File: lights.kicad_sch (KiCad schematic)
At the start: 24 parts, among them Q1 PMV60ENEAR, Q2 PMV60ENEAR

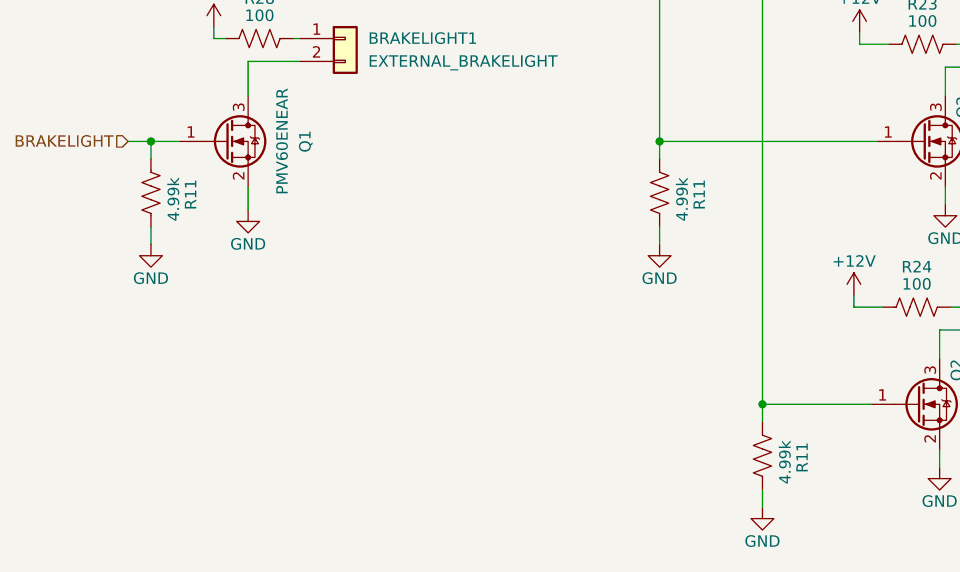
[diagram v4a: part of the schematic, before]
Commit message: organized schematic, changed resistor values, moved ignition signals to IC
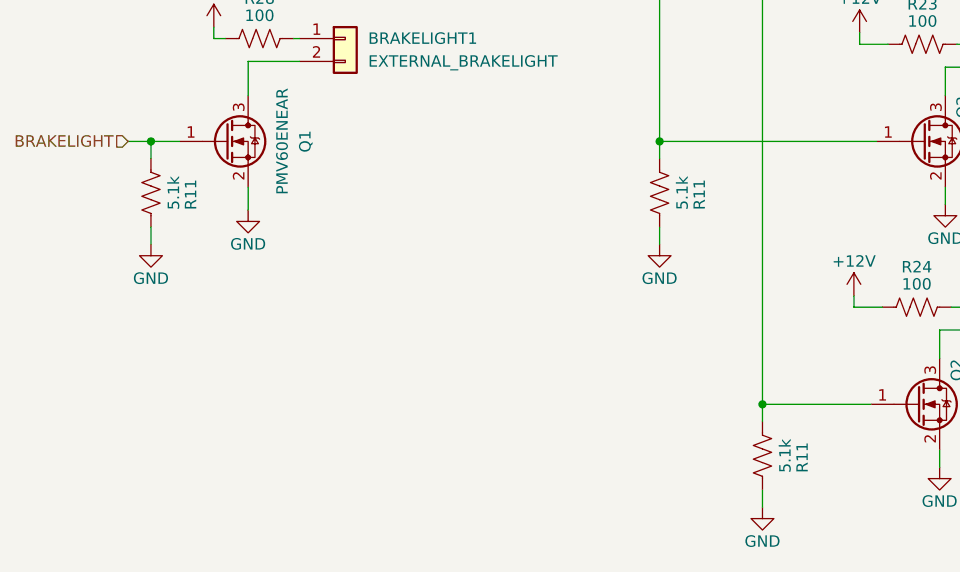
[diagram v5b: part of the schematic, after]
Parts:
- R11: value 4.99k -> 5.1k
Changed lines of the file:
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@@
       (effects (font (size 1.27 1.27)) (justify left))
     )
-    (property "Value" "4.99k" (at 98.425 129.54 90)
+    (property "Value" "5.1k" (at 98.425 128.27 90)
       (effects (font (size 1.27 1.27)) (justify left))
     )
@@
       (effects (font (size 1.27 1.27)) (justify left))
     )
-    (property "Value" "4.99k" (at 154.94 129.54 90)
+    (property "Value" "5.1k" (at 154.94 128.27 90)
       (effects (font (size 1.27 1.27)) (justify left))
     )
@@
       (effects (font (size 1.27 1.27)) (justify left))
     )
-    (property "Value" "4.99k" (at 166.37 158.75 90)
-      (effects (font (size 1.27 1.27)) (justify left))
-    )
+    (property "Value" "5.1k" (at 166.37 157.48 90)
+      (effects (font (size 1.27 1.27)) (justify left))
+    )

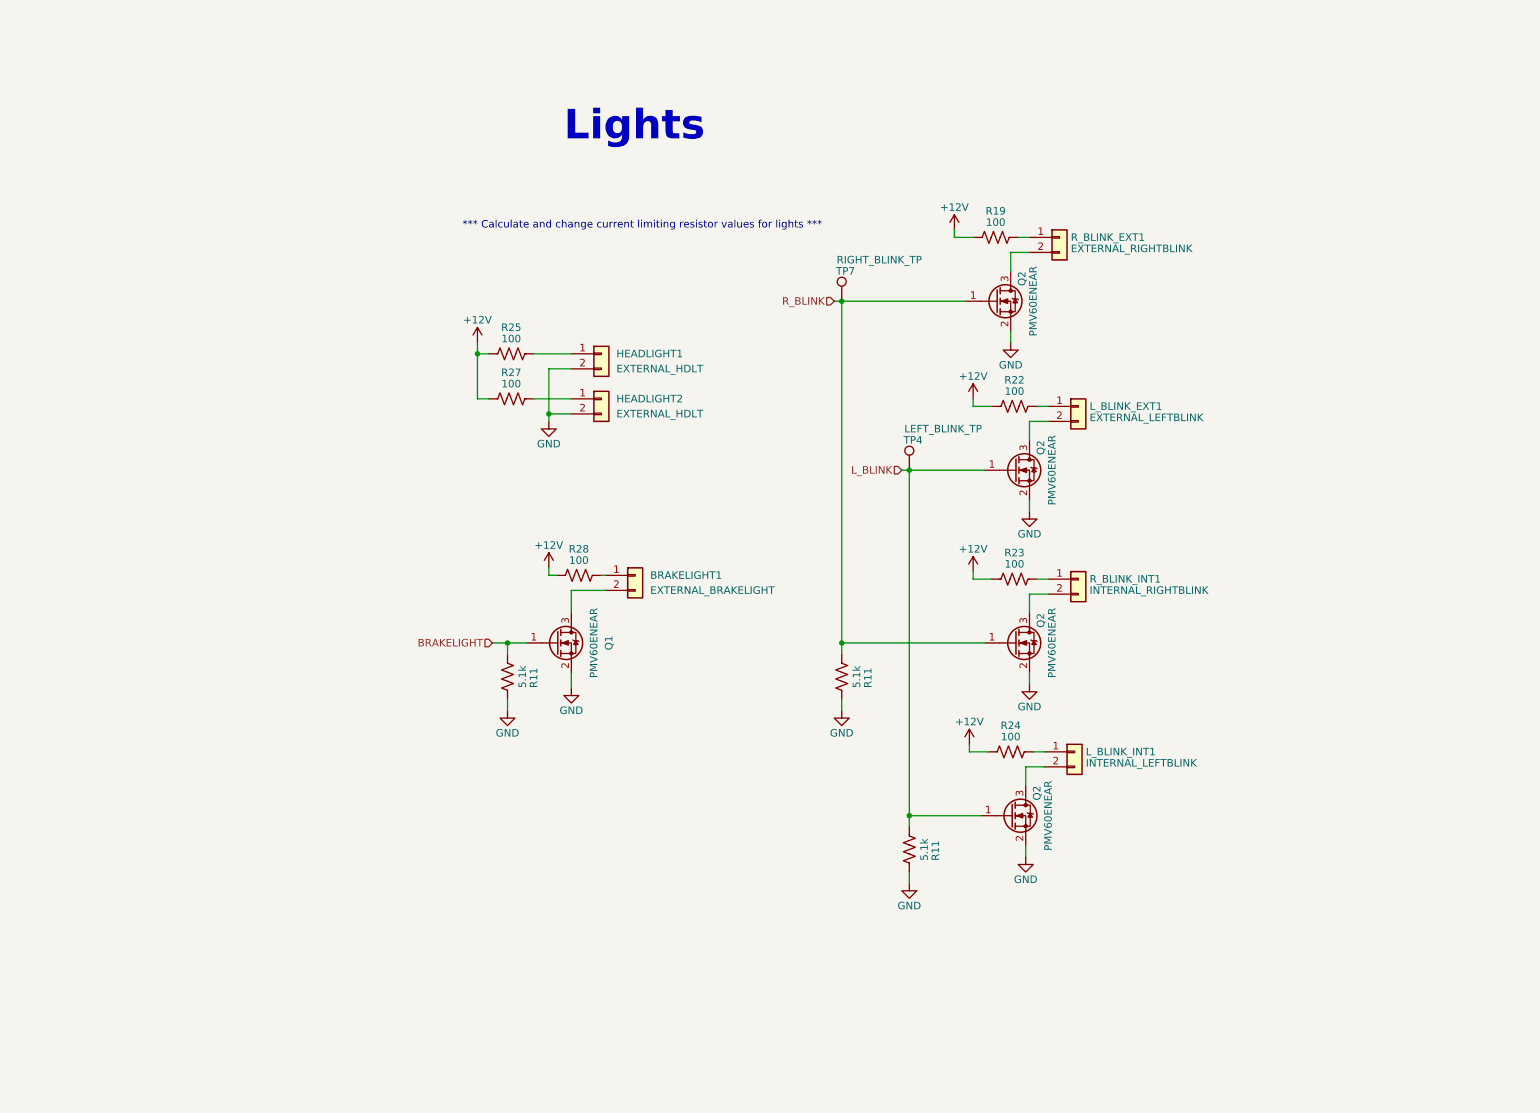
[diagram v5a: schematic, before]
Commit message: added notes section to bottom of sheets
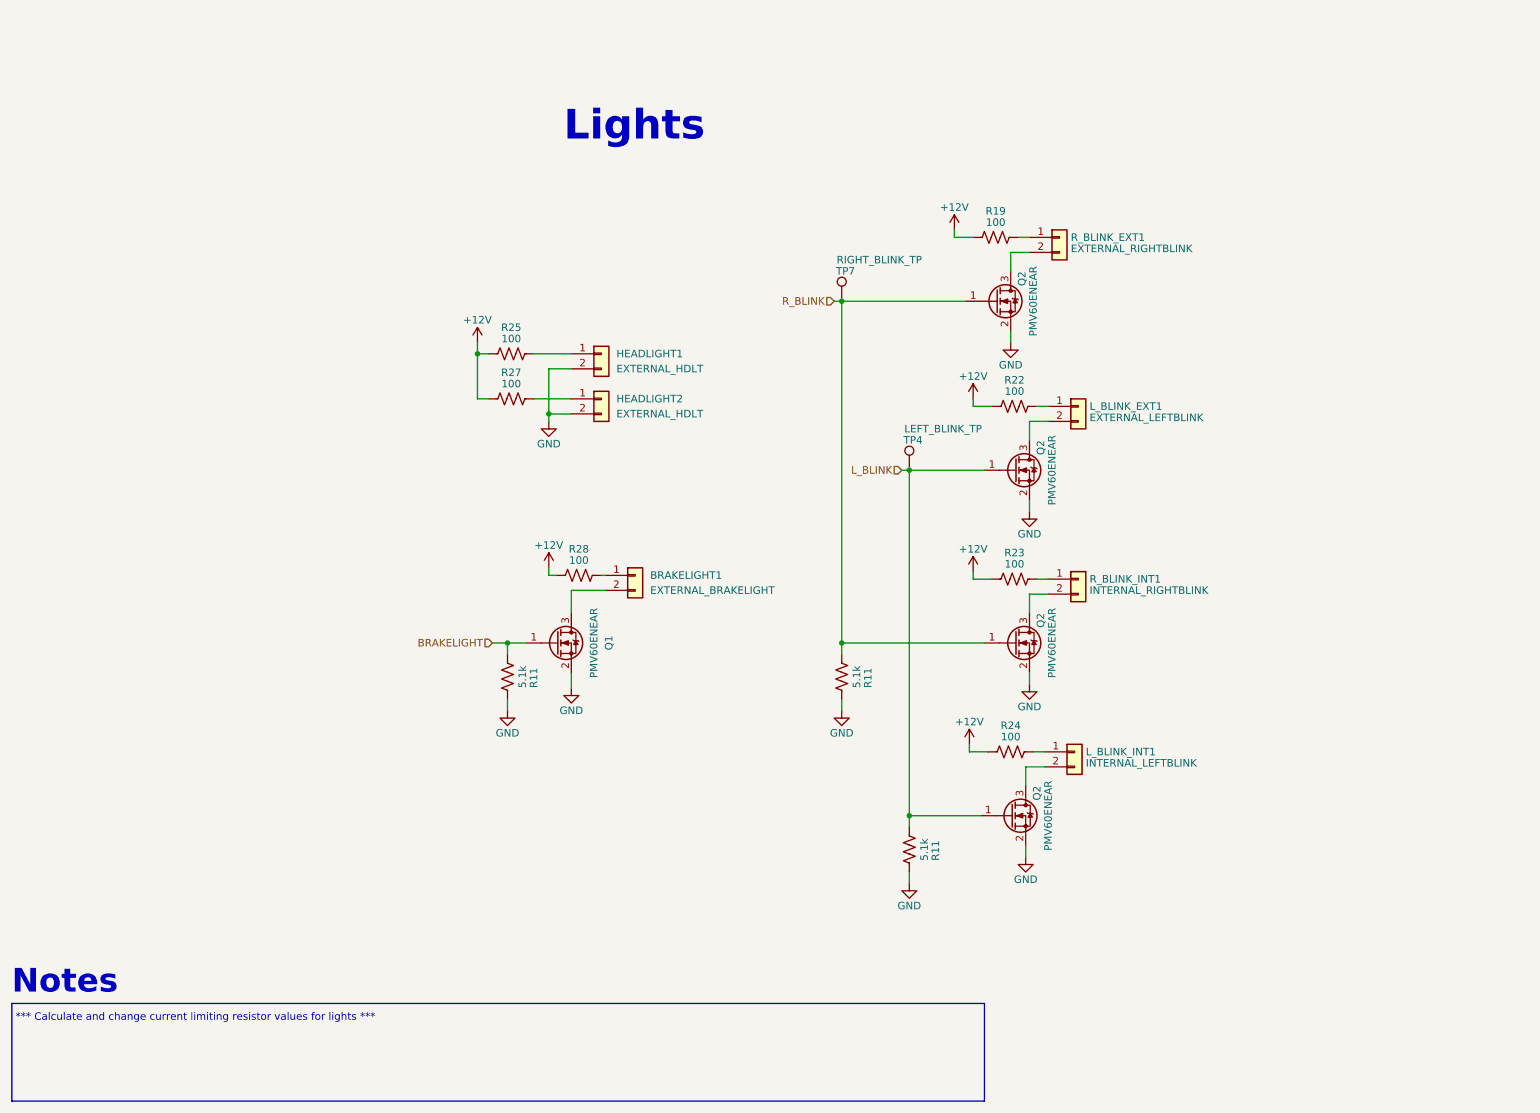
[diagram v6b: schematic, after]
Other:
- note added: "Notes"
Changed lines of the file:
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@@
     (stroke (width 0) (type default))
   )
+  (rectangle (start 12.065 181.61) (end 176.53 198.12)
+    (stroke (width 0) (type default))
+    (fill (type none))
+  )
+  (text "Notes" (at 12.065 180.34 0)
+    (effects (font (size 4 4) (thickness 0.8) bold) (justify left bottom))
+  )
   (text "*** Calculate and change current limiting resistor values for lights ***"
-    (at 88.265 50.8 0)
+    (at 12.7 184.785 0)
     (effects (font (size 1.27 1.27)) (justify left bottom))
   )

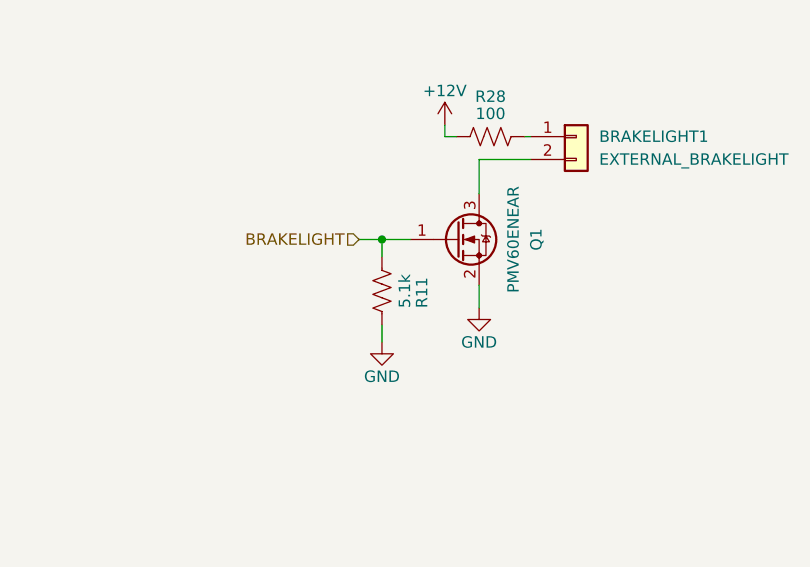
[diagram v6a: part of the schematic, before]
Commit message: Added to notes and changed resistor values
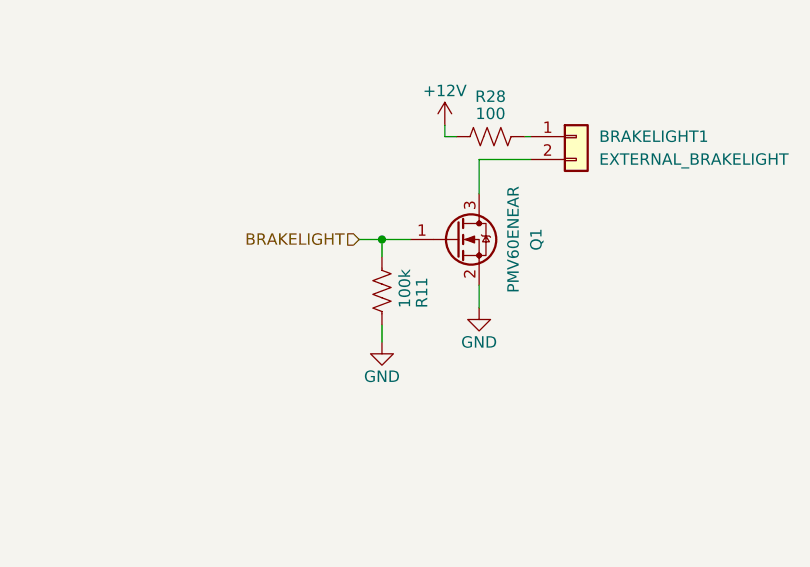
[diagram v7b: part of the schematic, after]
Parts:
- R11: value 5.1k -> 100k
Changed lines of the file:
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@@
       (effects (font (size 1.27 1.27)) (justify left))
     )
-    (property "Value" "5.1k" (at 98.425 128.27 90)
+    (property "Value" "100k" (at 98.425 128.27 90)
       (effects (font (size 1.27 1.27)) (justify left))
     )
